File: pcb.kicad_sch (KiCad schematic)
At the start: 4 parts

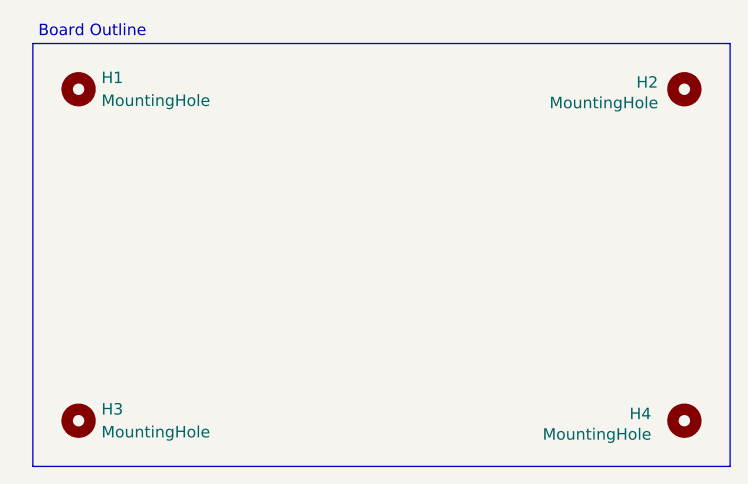
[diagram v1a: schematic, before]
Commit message: Adding in diodes and fixing circuit
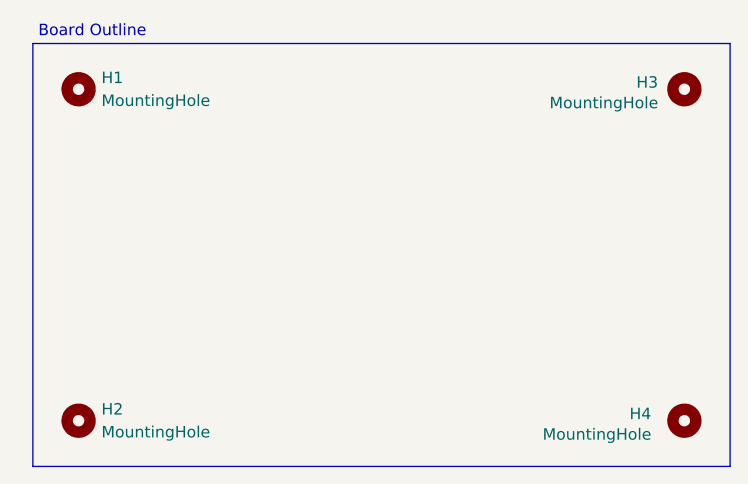
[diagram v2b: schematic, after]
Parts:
- renumbered H3 to H2, H2 to H3
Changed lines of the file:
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@@
 		(on_board yes)
 		(dnp no)
-		(property "Reference" "H2"
+		(property "Reference" "H3"
 			(at 163.576 56.388 0)
 			(effects
@@
 			(project "BMS"
 				(path "/124184ba-5d68-4d9f-8da6-acc6720ab30b/fb11fb4b-d26e-4f92-a711-2d1664bdbd55"
-					(reference "H2")
+					(reference "H3")
 					(unit 1)
 				)
@@
 		(dnp no)
 		(fields_autoplaced yes)
-		(property "Reference" "H3"
+		(property "Reference" "H2"
 			(at 104.14 92.7099 0)
 			(effects
@@
 			(project "BMS"
 				(path "/124184ba-5d68-4d9f-8da6-acc6720ab30b/fb11fb4b-d26e-4f92-a711-2d1664bdbd55"
-					(reference "H3")
+					(reference "H2")
 					(unit 1)
 				)

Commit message: Layed on board. Still need to route
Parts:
- removed H3, H4: MountingHole, symbol Mechanical:MountingHole
- H1, H2: footprint (none) -> MountingHole:MountingHole_2.2mm_M2_Pad_TopBottom
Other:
- moved on the sheet: H1

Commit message: Prelim placement done
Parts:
- added H3, H4: MountingHole, MountingHole:MountingHole_2.2mm_M2_Pad_TopBottom, symbol Mechanical:MountingHole
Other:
- moved on the sheet: H1, H2
